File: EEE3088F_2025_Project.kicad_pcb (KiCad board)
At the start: 2 copper layers, 79 x 57 mm, 46 parts, among them J1 Conn_02x16_Odd_Even, J2 USB_C_Receptacle_PowerOnly_6P, J3 Conn_01x02, Q2 NMOS, SW1 SW_SPDT, U1 HR8833, U10 INA219AIDCNR, U2 HR8833, U3 MIC2026-1YM, U4 HT7533-1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

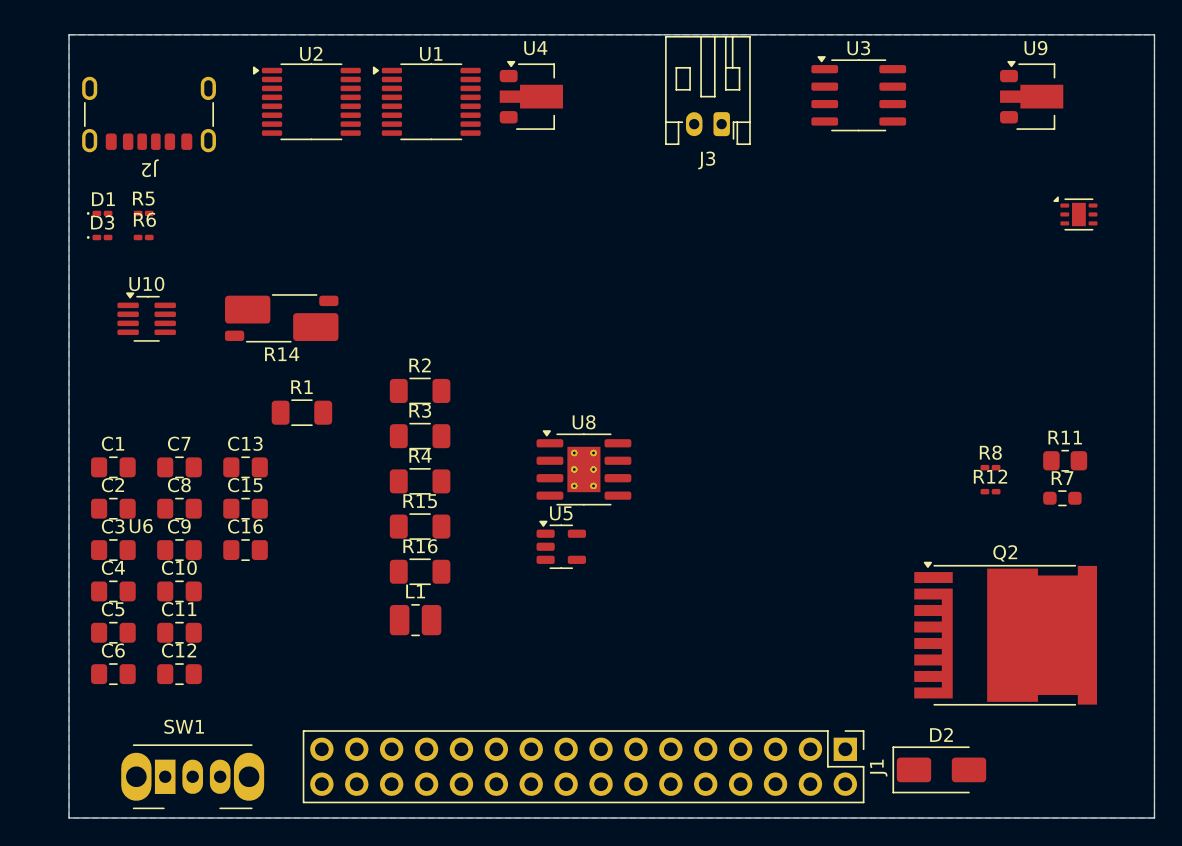
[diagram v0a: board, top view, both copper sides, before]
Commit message: Added testpoints and board layout shape
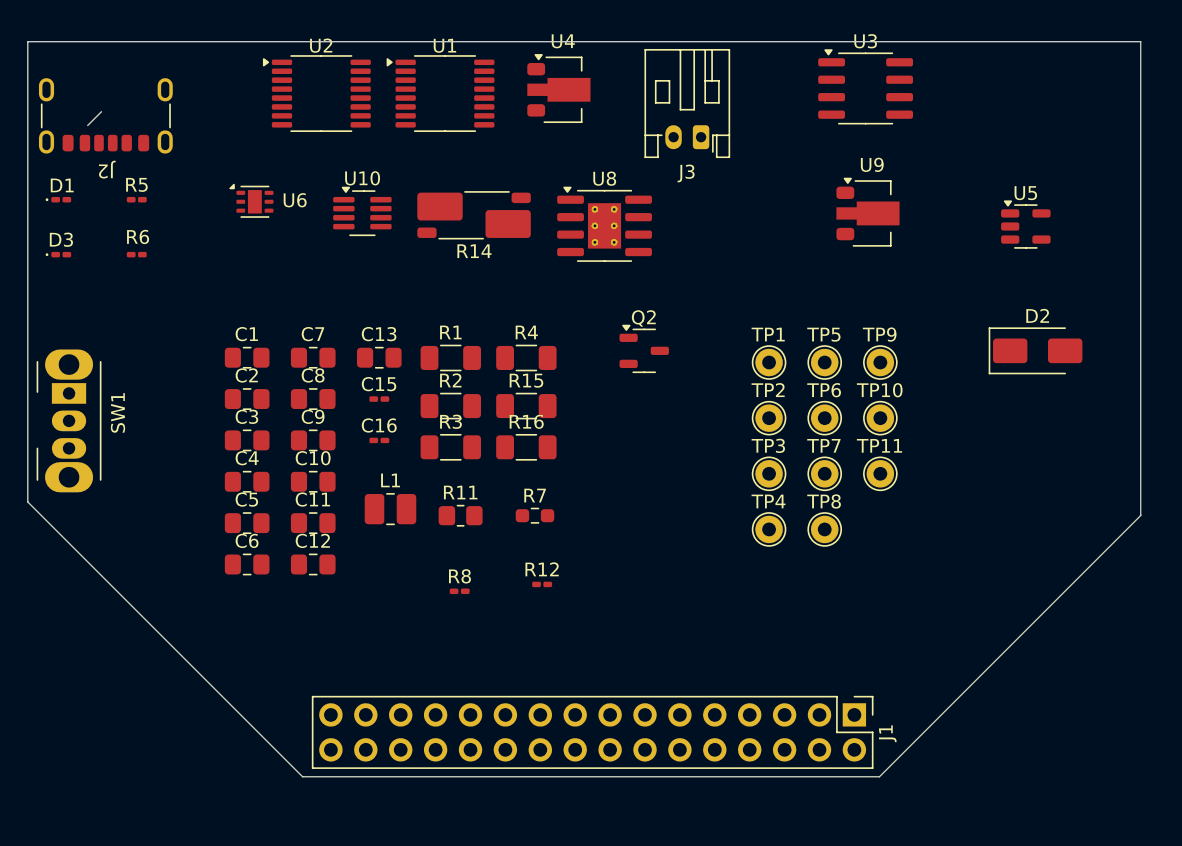
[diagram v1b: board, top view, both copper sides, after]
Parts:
- added TP1: TestPoint, TestPoint:TestPoint_THTPad_D2.0mm_Drill1.0mm, F.Cu at (97.5, 98.8)
- added TP10: TestPoint, TestPoint:TestPoint_THTPad_D2.0mm_Drill1.0mm, F.Cu at (105.5, 102.9)
- added TP11: TestPoint, TestPoint:TestPoint_THTPad_D2.0mm_Drill1.0mm, F.Cu at (105.5, 107.0)
- added TP2: TestPoint, TestPoint:TestPoint_THTPad_D2.0mm_Drill1.0mm, F.Cu at (97.5, 102.9)
- added TP3: TestPoint, TestPoint:TestPoint_THTPad_D2.0mm_Drill1.0mm, F.Cu at (97.5, 107.0)
- added TP4: TestPoint, TestPoint:TestPoint_THTPad_D2.0mm_Drill1.0mm, F.Cu at (97.5, 111.0)
- added TP5: TestPoint, TestPoint:TestPoint_THTPad_D2.0mm_Drill1.0mm, F.Cu at (101.5, 98.8)
- added TP6: TestPoint, TestPoint:TestPoint_THTPad_D2.0mm_Drill1.0mm, F.Cu at (101.5, 102.9)
- added TP7: TestPoint, TestPoint:TestPoint_THTPad_D2.0mm_Drill1.0mm, F.Cu at (101.5, 107.0)
- added TP8: TestPoint, TestPoint:TestPoint_THTPad_D2.0mm_Drill1.0mm, F.Cu at (101.5, 111.0)
- added TP9: TestPoint, TestPoint:TestPoint_THTPad_D2.0mm_Drill1.0mm, F.Cu at (105.5, 98.8)
- C15: footprint Capacitor_SMD:C_0805_2012Metric_Pad1.18x1.45mm_HandSolder -> Capacitor_SMD:C_0201_0603Metric_Pad0.64x0.40mm_HandSolder
- C16: value 10u -> 0.1u; footprint Capacitor_SMD:C_0805_2012Metric_Pad1.18x1.45mm_HandSolder -> Capacitor_SMD:C_0201_0603Metric_Pad0.64x0.40mm_HandSolder
- Q2: footprint Package_TO_SOT_SMD:Infineon_PG-HSOF-8-1 -> Package_TO_SOT_SMD:SOT-23-3
- moved U6 60.0 mm to (60.0, 87.2)
- moved R11 44.2 mm to (75.0, 110.0)
- moved U5 41.1 mm to (116.1, 89.0)
- moved R8 39.7 mm to (74.9, 115.5)
- moved R7 38.4 mm to (80.4, 110.0)
- moved Q2 33.5 mm to (88.4, 98.0)
- moved R12 33.3 mm to (80.9, 115.0)
- moved D2 31.3 mm to (117.0, 98.0)
- moved SW1 28.8 mm to (46.5, 101.1), turned to -90 degrees
- moved U8 17.8 mm to (85.5, 88.9)
- moved U10 17.5 mm to (67.8, 88.0)
- moved R14 15.9 mm to (76.0, 88.1)
- moved U9 14.6 mm to (105.0, 88.0)
- moved C1 12.6 mm to (59.5, 98.5)
- moved C13 12.6 mm to (69.1, 98.5)
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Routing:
- removed copper zone on B.Cu, net GND
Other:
- board size 79 x 57 mm -> 81 x 53.5 mm

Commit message: Added B.Cu layer as ground plane
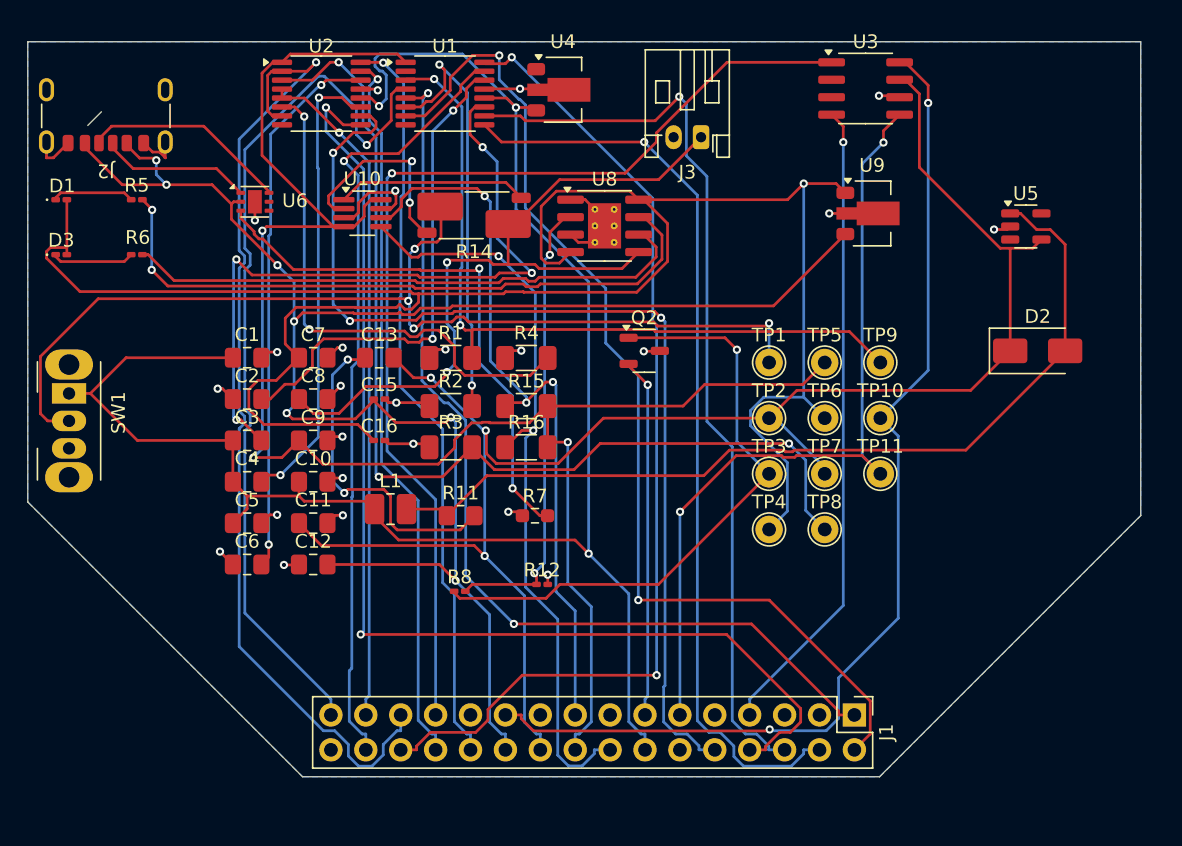
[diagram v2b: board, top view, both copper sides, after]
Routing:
- net /5V: track 0.00 -> 151.7 mm, vias 0 -> 1
- net /Battery: track 0.00 -> 132.3 mm, vias 0 -> 3
- net /HV: track 0.00 -> 128.0 mm, vias 0 -> 7
- net /3V3 Out: track 0.00 -> 126.4 mm, vias 0 -> 3
- net /5V Out: track 0.00 -> 124.3 mm, vias 0 -> 3
- net /MOTOR4_CTRL1: track 0.00 -> 82.6 mm, vias 0 -> 2
- net /EXT_LOAD1_OUT: track 0.00 -> 78.0 mm, vias 0 -> 2
- net /Motor2_A_OUT: track 0.00 -> 77.0 mm, vias 0 -> 2
- net /CTRL_EXT_LOAD1: track 0.00 -> 76.8 mm, vias 0 -> 1
- net /MOTOR4_CTRL2: track 0.00 -> 75.8 mm, vias 0 -> 3
- net Net-(U2-AISEN): track 0.00 -> 75.6 mm, vias 0 -> 3
- net Net-(SW1-B): track 0.00 -> 75.2 mm, vias 0 -> 4
- net /MOTOR1_CTRL1: track 0.00 -> 73.1 mm, vias 0 -> 2
- net /MOTOR3_A_OUT: track 0.00 -> 71.7 mm, vias 0 -> 1
- net /Motor2_B_OUT: track 0.00 -> 71.2 mm, vias 0 -> 2
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- added copper zone on B.Cu, net GND

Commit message: Added mounting holes
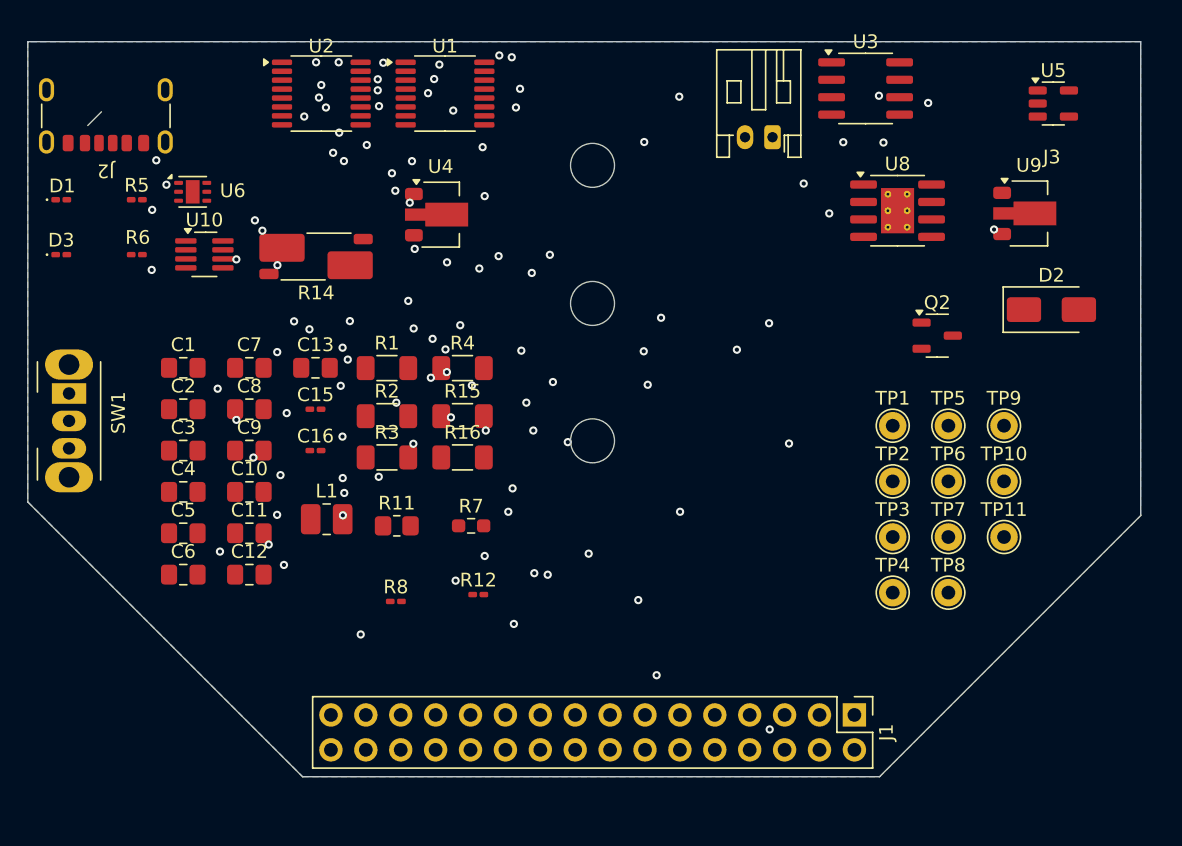
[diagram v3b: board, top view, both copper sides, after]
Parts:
- moved Q2 21.4 mm to (109.7, 96.9)
- moved U8 21.4 mm to (106.8, 87.8)
- moved U4 12.7 mm to (73.5, 88.1)
- moved R14 11.9 mm to (64.5, 91.1)
- moved U10 11.9 mm to (56.4, 91.0)
- moved U9 11.4 mm to (116.4, 88.0)
- moved TP1 10.1 mm to (106.5, 103.5)
- moved TP5 10.1 mm to (110.5, 103.5)
- moved TP9 10.1 mm to (114.5, 103.5)
- moved TP10 10.1 mm to (114.5, 107.5)
- moved TP11 10.1 mm to (114.5, 111.5)
- moved TP2 10.1 mm to (106.5, 107.5)
- moved TP3 10.1 mm to (106.5, 111.5)
- moved TP4 10.1 mm to (106.5, 115.6)
- moved TP6 10.1 mm to (110.5, 107.5)
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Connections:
- net Net-(U10-IN+) renamed /IN+
- net Net-(U10-IN-) renamed /IN-
- J3 pad 1: /Vbat -> GND
- J3 pad 2: GND -> /Vbat
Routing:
- net /5V: track 151.7 -> 0.00 mm
- net /Battery: track 132.3 -> 0.00 mm
- net /HV: track 128.0 -> 0.00 mm, vias 7 -> 10
- net /3V3 Out: track 126.4 -> 0.00 mm, vias 3 -> 4
- net /5V Out: track 124.3 -> 0.00 mm, vias 3 -> 2
- net /MOTOR4_CTRL1: track 82.6 -> 0.00 mm
- net /EXT_LOAD1_OUT: track 78.0 -> 0.00 mm
- net /Motor2_A_OUT: track 77.0 -> 0.00 mm
- net /CTRL_EXT_LOAD1: track 76.8 -> 0.00 mm
- net /MOTOR4_CTRL2: track 75.8 -> 0.00 mm
- net Net-(U2-AISEN): track 75.6 -> 0.00 mm, vias 3 -> 5
- net Net-(SW1-B): track 75.2 -> 0.00 mm
- net /MOTOR1_CTRL1: track 73.1 -> 0.00 mm
- net /MOTOR3_A_OUT: track 71.7 -> 0.00 mm
- net /Motor2_B_OUT: track 71.2 -> 0.00 mm, vias 2 -> 3
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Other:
- outline, holes or cut-outs redrawn
